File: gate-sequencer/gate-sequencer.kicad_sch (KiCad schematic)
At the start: 109 parts, among them J1 Gate 8, J10 Gate 6, J11 Gate 10, J12 Gate 14, J13 Gate 1, J14 Gate 5, J15 Gate 9, J16 Gate 13, J2 Gate 4, J3 Gate 12, J4 Gate 16, J5 Gate 3, J6 Gate 7, J7 Gate 11, J8 Gate 15, J9 Gate 2, SW1 X1, SW10 S6, SW11 S7, SW12 S8, SW13 S9, SW14 S10, SW15 S11, SW16 S12, SW17 S13, SW18 S14, SW19 S15, SW2 X2, SW20 S16, SW3 X3, SW35 Mode, SW4 X4, SW5 S1, SW6 S2, SW7 S3, SW8 S4, SW9 S5

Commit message: Updates
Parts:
- removed C1: 100nf, Capacitor_THT:C_Disc_D4.3mm_W1.9mm_P5.00mm, symbol Device:C_Small
- added C3: 100nf, Capacitor_THT:C_Disc_D4.3mm_W1.9mm_P5.00mm, symbol Device:C_Small
- added J17, J22: Clock, modular2:banana-jack, symbol Connector:Conn_01x01_Pin
- added J18: Conn_01x34_Socket, Connector_PinSocket_2.54mm:PinSocket_1x34_P2.54mm_Vertical, symbol Connector:Conn_01x34_Socket
- added J19, J20, J21: Power, Connector_IDC:IDC-Header_2x03_P2.54mm_Vertical, symbol Connector_Generic:Conn_02x03_Odd_Even
- added J23: Gate 1, modular2:banana-jack, symbol Connector:Conn_01x01_Pin
- added J24: Gate 9, modular2:banana-jack, symbol Connector:Conn_01x01_Pin
- added J25: Gate 2, modular2:banana-jack, symbol Connector:Conn_01x01_Pin
- added J26: Gate 10, modular2:banana-jack, symbol Connector:Conn_01x01_Pin
- added J27: Gate 3, modular2:banana-jack, symbol Connector:Conn_01x01_Pin
- added J28: Gate 11, modular2:banana-jack, symbol Connector:Conn_01x01_Pin
- added J29: Gate 4, modular2:banana-jack, symbol Connector:Conn_01x01_Pin
- added J30: Gate 12, modular2:banana-jack, symbol Connector:Conn_01x01_Pin
- added J31: Gate 5, modular2:banana-jack, symbol Connector:Conn_01x01_Pin
- added J32: Gate 13, modular2:banana-jack, symbol Connector:Conn_01x01_Pin
- added J33: Gate 6, modular2:banana-jack, symbol Connector:Conn_01x01_Pin
- added J34: Gate 14, modular2:banana-jack, symbol Connector:Conn_01x01_Pin
- added J35: Gate 7, modular2:banana-jack, symbol Connector:Conn_01x01_Pin
- added J36: Gate 15, modular2:banana-jack, symbol Connector:Conn_01x01_Pin
- added J37: Gate 8, modular2:banana-jack, symbol Connector:Conn_01x01_Pin
- added J38: Gate 16, modular2:banana-jack, symbol Connector:Conn_01x01_Pin
- added J39, J40, J41, J42, J43, J44, J45, J46, J47, J48, J49, J50, J51, J52, J53, J54: LED, Connector_PinHeader_2.54mm:PinHeader_1x02_P2.54mm_Vertical, symbol Connector:Conn_01x02_Pin
- added J55: Conn_01x34_Pin, Connector_PinHeader_2.54mm:PinHeader_1x34_P2.54mm_Vertical, symbol Connector:Conn_01x34_Pin
- added R33: 1K, Resistor_THT:R_Axial_DIN0207_L6.3mm_D2.5mm_P10.16mm_Horizontal, symbol Device:R_US
- added RV1: 100K - Tempo, Potentiometer_THT:Potentiometer_Alps_RK09K_Single_Vertical, symbol Device:R_Potentiometer_US
- added RV2: 100K - Period, Potentiometer_THT:Potentiometer_Alps_RK09K_Single_Vertical, symbol Device:R_Potentiometer_US
- added SW21: Mode, modular2:switch1, symbol Switch:SW_Nidec_CAS-120A1
- added SW22: Mode 2, modular2:switch1, symbol Switch:SW_Nidec_CAS-120A1
- SW35: value Mode -> Clock Source
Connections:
- net 5V: now also J19.5 (Pin_5), J20.5 (Pin_5), J21.5 (Pin_5), RV1.3, RV2.3
- net GND: now also SW35.3 (A), C3.1, J18.34 (Pin_34), J19.3 (Pin_3), J19.4 (Pin_4), J20.3 (Pin_3), J20.4 (Pin_4), J21.3 (Pin_3), J21.4 (Pin_4), RV1.1, RV2.1, SW21.3 (A), SW22.3 (A)
- net at J9.1 (Pin_1), R18.1: now also J18.5 (Pin_5)
- net at D27.2 (A), R15.1: now also J18.28 (Pin_28)
- net at SW35.2 (B): now also A1.2 (D0/RX)
- net at SW5.2, SW6.2, SW7.2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: now also A1.9 (D6)
- net at D25.2 (A), R11.1: now also J18.26 (Pin_26)
- net at D24.2 (A), R9.1: now also J18.10 (Pin_10)
- net at D22.2 (A), R4.1: now also J18.16 (Pin_16)
- net at SW10.2, SW11.2, SW12.2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: now also A1.8 (D5)
- net at D23.2 (A), R6.1: now also J18.32 (Pin_32)
- net at SW17.2, SW18.2, SW19.2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: now also A1.6 (D3)
- net at J8.1 (Pin_1), R16.1: now also J18.27 (Pin_27)
- net at J15.1 (Pin_1), R30.1: now also J18.3 (Pin_3)
- net at D12.1 (K), D16.1 (K), D20.1 (K)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: now also A1.14 (D11)
- net at J1.1 (Pin_1), R3.1: now also J18.29 (Pin_29)
- net at SW1.2, SW2.2, SW3.2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: now also A1.10 (D7)
- net at D10.1 (K), D14.1 (K), D18.1 (K)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: now also A1.12 (D9)
- net at SW13.2, SW14.2, SW15.2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: now also A1.7 (D4)
- net at J10.1 (Pin_1), R20.1: now also J18.21 (Pin_21)
- net at D1.1 (K), D13.1 (K), D17.1 (K)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: now also A1.11 (D8)
- net at D34.2 (A), R27.1: now also J18.18 (Pin_18)
- net at J4.1 (Pin_1), R7.1: now also J18.31 (Pin_31)
- net at D31.2 (A), R23.1: now also J18.24 (Pin_24)
- net at J5.1 (Pin_1), R10.1: now also J18.9 (Pin_9)
- net at D26.2 (A), R13.1: now also J18.12 (Pin_12)
- net at J11.1 (Pin_1), R22.1: now also J18.7 (Pin_7)
- net at D35.2 (A), R29.1: now also J18.4 (Pin_4)
- net at J14.1 (Pin_1), R28.1: now also J18.17 (Pin_17)
- net at D11.1 (K), D15.1 (K), D19.1 (K)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: now also A1.13 (D10)
- net at J3.1 (Pin_1), R5.1: now also J18.15 (Pin_15)
- net at J6.1 (Pin_1), R12.1: now also J18.25 (Pin_25)
- net at D33.2 (A), R25.1: now also J18.2 (Pin_2)
- net at U1.1 (STROBE): now also A1.24 (A5)
- net at U1.2 (A): now also A1.19 (A0)
- net at U1.21 (C): now also A1.21 (A2)
- net at U1.22 (D): now also A1.22 (A3)
- net at U1.23 (INHIBIT): now also A1.23 (A4)
- net at U1.3 (B): now also A1.20 (A1)
- net at J12.1 (Pin_1), R24.1: now also J18.23 (Pin_23)
- net at J13.1 (Pin_1), R26.1: now also J18.1 (Pin_1)
- net at A1.1 (D1/TX): now also SW21.2 (B)
- net at A1.15 (D12): now also SW22.2 (B)
- net at A1.18 (AREF): now also C3.2
- net at A1.25 (A6): now also RV1.2
- net at A1.26 (A7): now also RV2.2
- net at A1.5 (D2): now also R33.2
- net at D28.2 (A), R17.1: now also J18.6 (Pin_6)
- net at D21.2 (A), R2.1: now also J18.30 (Pin_30)
- net at D30.2 (A), R21.1: now also J18.8 (Pin_8)
- net at J16.1 (Pin_1), R32.1: now also J18.19 (Pin_19)
- net at D29.2 (A), R19.1: now also J18.22 (Pin_22)
- net at J7.1 (Pin_1), R14.1: now also J18.11 (Pin_11)
- net at D32.2 (A), R8.1: now also J18.14 (Pin_14)
- net at D36.2 (A), R31.1: now also J18.20 (Pin_20)
- net at J2.1 (Pin_1), R1.1: now also J18.13 (Pin_13)
- new net: J33.1 (Pin_1), J55.21 (Pin_21)
- new net: J32.1 (Pin_1), J55.19 (Pin_19)
- new net: J44.1 (Pin_1), J55.12 (Pin_12)
- new net: J39.2 (Pin_2), J40.2 (Pin_2), J41.2 (Pin_2), J42.2 (Pin_2), J43.2 (Pin_2), J44.2 (Pin_2), J45.2 (Pin_2), J46.2 (Pin_2), J47.2 (Pin_2), J48.2 (Pin_2), J49.2 (Pin_2), J50.2 (Pin_2), J51.2 (Pin_2), J52.2 (Pin_2), J53.2 (Pin_2), J54.2 (Pin_2), J55.34 (Pin_34)
- new net: J53.1 (Pin_1), J55.30 (Pin_30)
- new net: J34.1 (Pin_1), J55.23 (Pin_23)
- new net: J23.1 (Pin_1), J55.1 (Pin_1)
- new net: J37.1 (Pin_1), J55.29 (Pin_29)
- new net: J36.1 (Pin_1), J55.27 (Pin_27)
- new net: J27.1 (Pin_1), J55.9 (Pin_9)
- new net: J41.1 (Pin_1), J55.6 (Pin_6)
- new net: J43.1 (Pin_1), J55.10 (Pin_10)
- new net: J28.1 (Pin_1), J55.11 (Pin_11)
- new net: J29.1 (Pin_1), J55.13 (Pin_13)
- new net: J45.1 (Pin_1), J55.14 (Pin_14)
- new net: J30.1 (Pin_1), J55.15 (Pin_15)
- new net: J46.1 (Pin_1), J55.16 (Pin_16)
- new net: J31.1 (Pin_1), J55.17 (Pin_17)
- new net: J47.1 (Pin_1), J55.18 (Pin_18)
- new net: J39.1 (Pin_1), J55.2 (Pin_2)
- new net: J48.1 (Pin_1), J55.20 (Pin_20)
- new net: J49.1 (Pin_1), J55.22 (Pin_22)
- new net: J50.1 (Pin_1), J55.24 (Pin_24)
- new net: J35.1 (Pin_1), J55.25 (Pin_25)
- new net: J51.1 (Pin_1), J55.26 (Pin_26)
- new net: J52.1 (Pin_1), J55.28 (Pin_28)
- new net: J24.1 (Pin_1), J55.3 (Pin_3)
- new net: J38.1 (Pin_1), J55.31 (Pin_31)
- new net: J54.1 (Pin_1), J55.32 (Pin_32)
- new net: J22.1 (Pin_1), J55.33 (Pin_33)
- new net: J40.1 (Pin_1), J55.4 (Pin_4)
- new net: J25.1 (Pin_1), J55.5 (Pin_5)
- new net: J26.1 (Pin_1), J55.7 (Pin_7)
- new net: J42.1 (Pin_1), J55.8 (Pin_8)
- new net: J17.1 (Pin_1), J18.33 (Pin_33), R33.1
- new net -12V: J19.2 (Pin_2), J20.2 (Pin_2), J21.2 (Pin_2)
- new net 12V: J19.1 (Pin_1), J20.1 (Pin_1), J21.1 (Pin_1)
- no-connect marks 5 -> 8
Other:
- moved on the sheet: J1, J10, J11, J12, J13, J14, J15, J16, J2, J3, J4, J5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

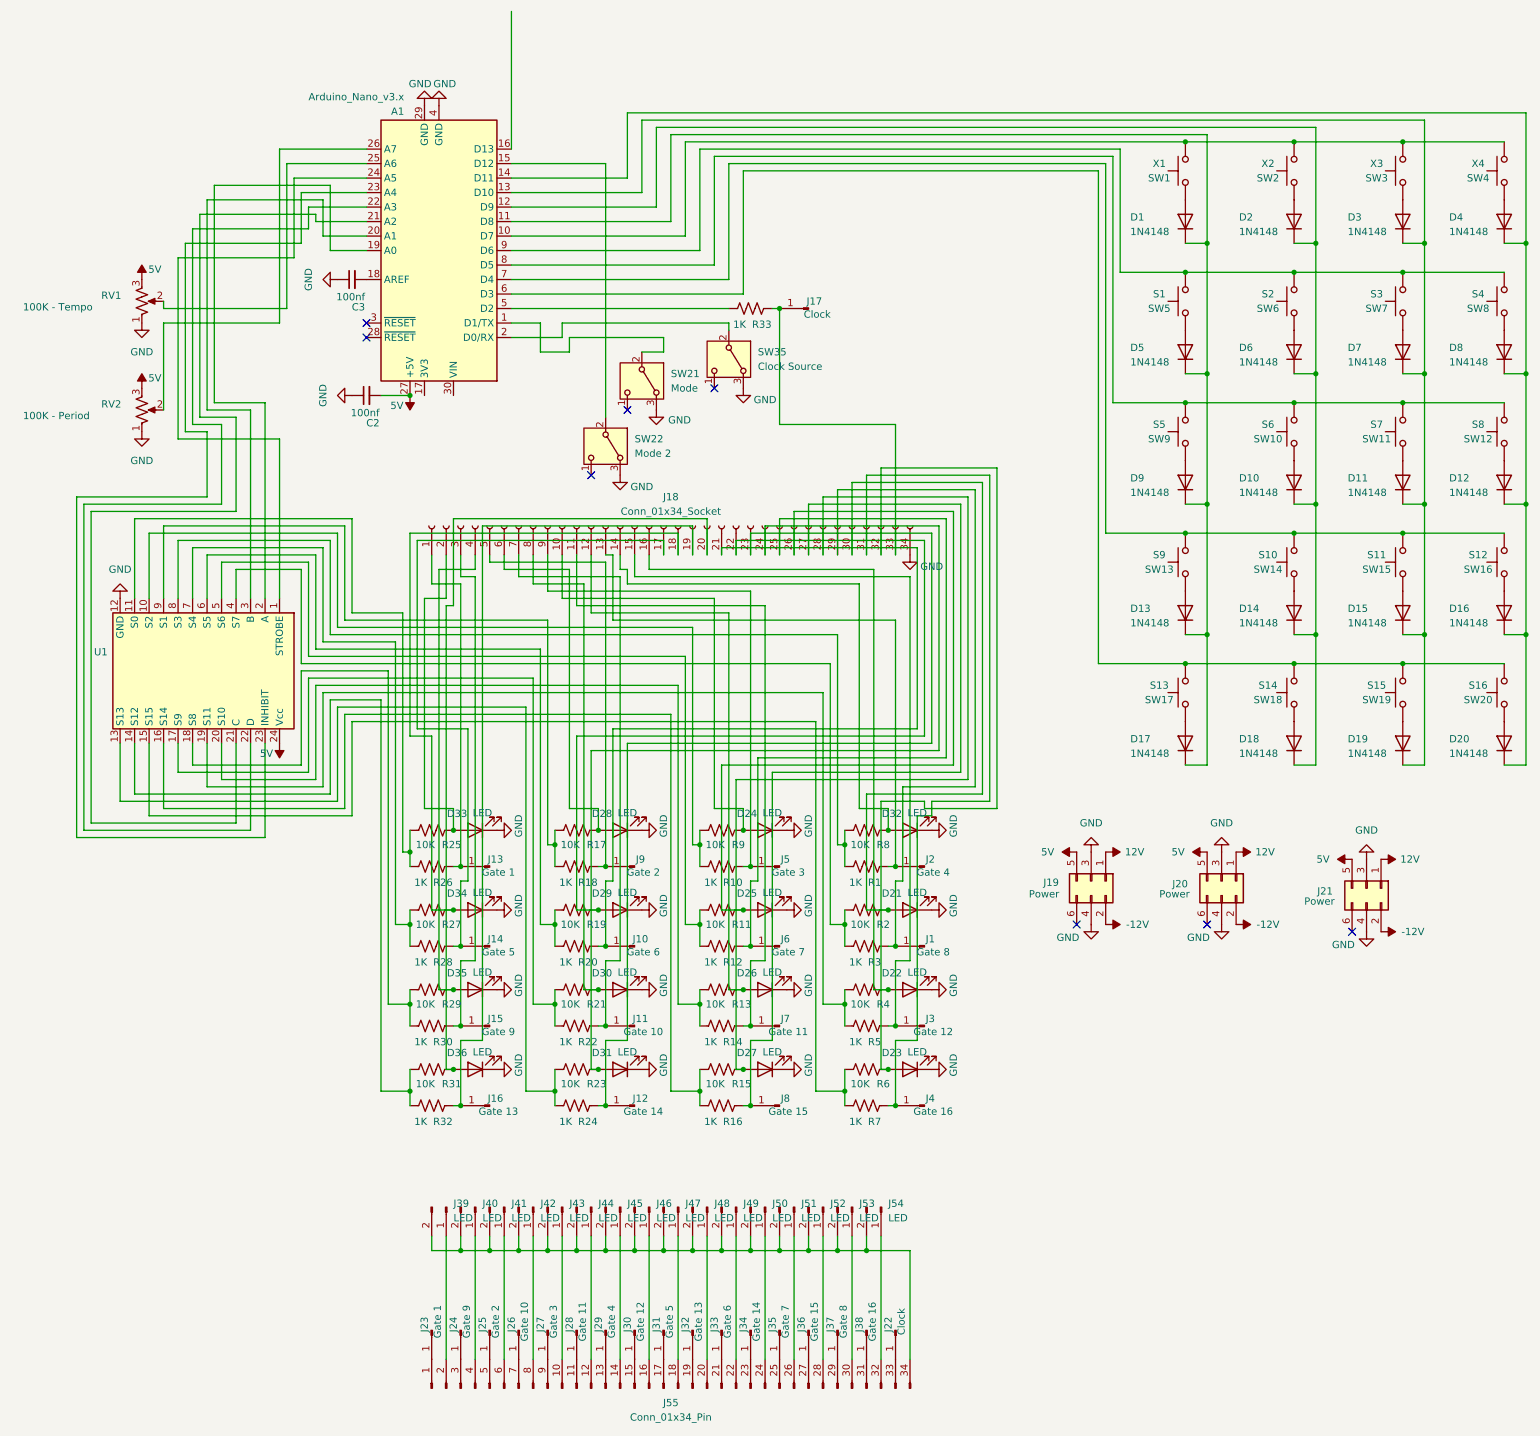
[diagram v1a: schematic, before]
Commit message: Renumber some components
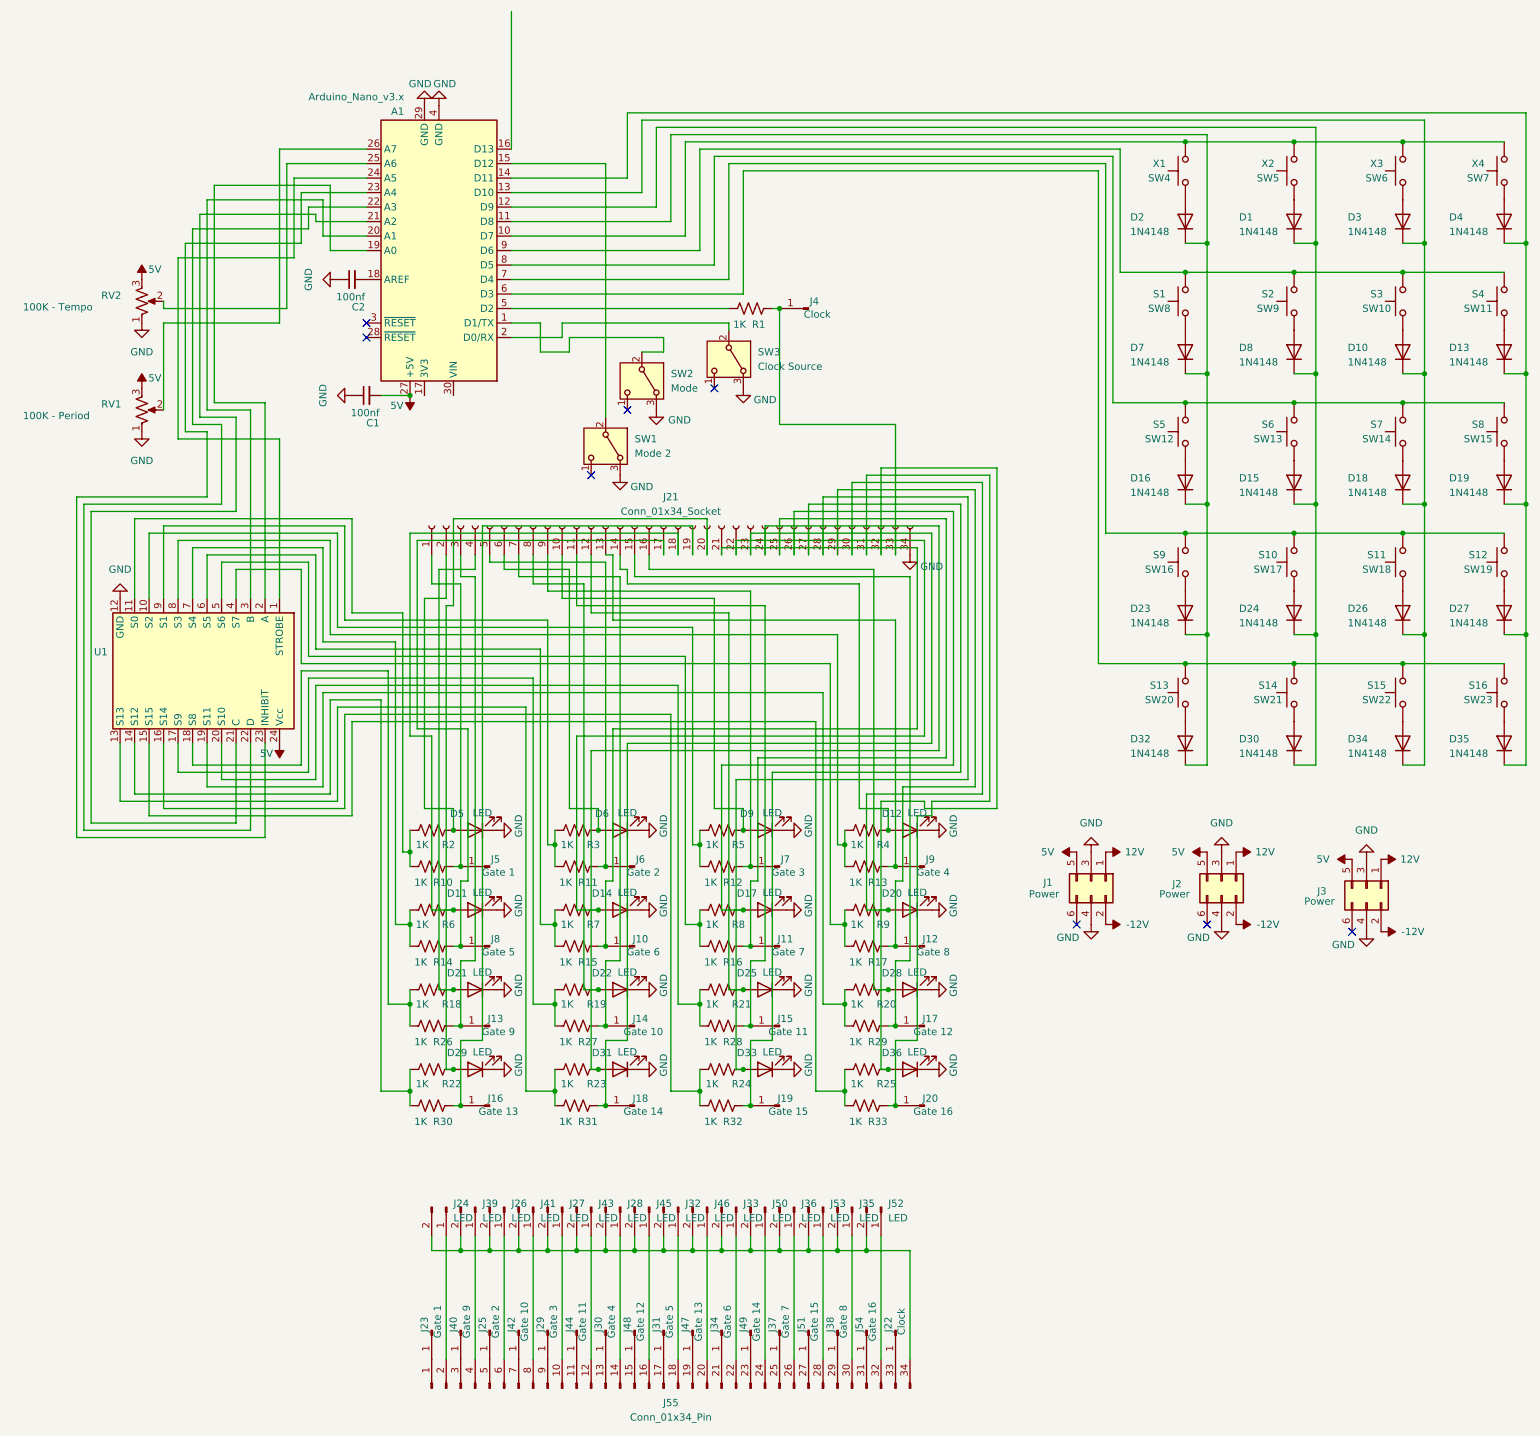
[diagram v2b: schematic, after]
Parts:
- R18: renamed from R29; value 10K -> 1K
- R19: renamed from R21; value 10K -> 1K
- R2: renamed from R25; value 10K -> 1K
- R20: renamed from R4; value 10K -> 1K
- R21: renamed from R13; value 10K -> 1K
- R22: renamed from R31; value 10K -> 1K
- R23: value 10K -> 1K
- R24: renamed from R15; value 10K -> 1K
- R25: renamed from R6; value 10K -> 1K
- R3: renamed from R17; value 10K -> 1K
- R4: renamed from R8; value 10K -> 1K
- R5: renamed from R9; value 10K -> 1K
- R6: renamed from R27; value 10K -> 1K
- R7: renamed from R19; value 10K -> 1K
- R8: renamed from R11; value 10K -> 1K
- R9: renamed from R2; value 10K -> 1K
- renumbered C2 to C1, C3 to C2, D2 to D1, D7 to D10, D34 to D11, D32 to D12, D8 to D13, D29 to D14, D10 to D15, D9 to D16, D25 to D17, D11 to D18, D12 to D19, D1 to D2, D21 to D20, D35 to D21, D30 to D22, D13 to D23, D14 to D24, D26 to D25, D15 to D26, D16 to D27, D22 to D28, D36 to D29, D18 to D30, D17 to D32, D27 to D33, D19 to D34, D20 to D35, D23 to D36, D33 to D5, D28 to D6, D5 to D7, D6 to D8, D24 to D9, J19 to J1, J6 to J11, J1 to J12, J15 to J13, J11 to J14, J7 to J15, J3 to J17, J12 to J18, J8 to J19, J20 to J2, J4 to J20, J18 to J21, J39 to J24, J41 to J26, J43 to J27, J45 to J28, J27 to J29, J21 to J3, J29 to J30, J47 to J32, J49 to J33, J33 to J34, J53 to J35, J51 to J36, J35 to J37, J37 to J38, J40 to J39, J17 to J4, J24 to J40, J42 to J41, J26 to J42, J44 to J43, J28 to J44, J46 to J45, J48 to J46, J32 to J47, J30 to J48, J34 to J49, J13 to J5, J36 to J51, J54 to J52, J52 to J53, J38 to J54, J9 to J6, J5 to J7, J14 to J8, J2 to J9, R33 to R1, R26 to R10, R18 to R11, R10 to R12, R1 to R13, R28 to R14, R20 to R15, R12 to R16, R3 to R17, R30 to R26, R22 to R27, R14 to R28, R5 to R29, R32 to R30, R24 to R31, R16 to R32, R7 to R33, RV2 to RV1, RV1 to RV2, SW22 to SW1, SW7 to SW10, SW8 to SW11, SW9 to SW12, SW10 to SW13, SW11 to SW14, SW12 to SW15, SW13 to SW16, SW14 to SW17, SW15 to SW18, SW16 to SW19, SW21 to SW2, SW17 to SW20, SW18 to SW21, SW19 to SW22, SW20 to SW23, SW35 to SW3, SW1 to SW4, SW2 to SW5, SW3 to SW6, SW4 to SW7, SW5 to SW8, SW6 to SW9

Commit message: Update some designs
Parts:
- U1: value ~ -> (none)

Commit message: Gate sequencer fixes
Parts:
- added D37, D38, D39, D40, D41, D42, D43, D44, D45, D46, D47, D48, D49, D50, D51, D52: 1N4148, Diode_THT:D_DO-35_SOD27_P7.62mm_Horizontal, symbol Diode:1N4148
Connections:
- net at R5.2, U1.10 (S2): now also D45.2 (A); no longer R12.2
- net at R20.2, U1.19 (S11): now also D51.2 (A); no longer R29.2
- net at R24.2, U1.16 (S14): now also D48.2 (A); no longer R32.2
- net at R9.2, U1.4 (S7): now also D50.2 (A); no longer R17.2
- net at R25.2, U1.15 (S15): now also D52.2 (A); no longer R33.2
- net at R23.2, U1.13 (S13): now also D44.2 (A); no longer R31.2
- net at R19.2, U1.17 (S9): now also D41.2 (A); no longer R27.2
- net at R18.2, U1.18 (S8): now also D39.2 (A); no longer R26.2
- net at R7.2, U1.6 (S5): now also D42.2 (A); no longer R15.2
- net at R8.2, U1.5 (S6): now also D46.2 (A); no longer R16.2
- net at R2.2, U1.11 (S0): now also D37.2 (A); no longer R10.2
- net at R22.2, U1.14 (S12): now also D40.2 (A); no longer R30.2
- net at R21.2, U1.20 (S10): now also D47.2 (A); no longer R28.2
- net at R6.2, U1.7 (S4): now also D38.2 (A); no longer R14.2
- net at R4.2, U1.8 (S3): now also D49.2 (A); no longer R13.2
- net at R3.2, U1.9 (S1): now also D43.2 (A); no longer R11.2
- new net: D41.1 (K), R27.2
- new net: D45.1 (K), R12.2
- new net: D50.1 (K), R17.2
- new net: D48.1 (K), R32.2
- new net: D40.1 (K), R30.2
- new net: D49.1 (K), R13.2
- new net: D52.1 (K), R33.2
- new net: D39.1 (K), R26.2
- new net: D38.1 (K), R14.2
- new net: D42.1 (K), R15.2
- new net: D46.1 (K), R16.2
- new net: D44.1 (K), R31.2
- new net: D51.1 (K), R29.2
- new net: D43.1 (K), R11.2
- new net: D47.1 (K), R28.2
- new net: D37.1 (K), R10.2
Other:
- moved on the sheet: J10, J11, J12, J13, J14, J15, J16, J17, J18, J19, J20, J5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
